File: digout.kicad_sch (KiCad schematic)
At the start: 24 parts, among them J11 EPY.00.250.NTN, J12 EPY.00.250.NTN, J13 EPY.00.250.NTN, J14 EPY.00.250.NTN, U13 SN74LVC8T245PW, U14 SN74LVC8T245PW, U15 SN74LVC8T245PW, U5 SN74LVC8T245PW

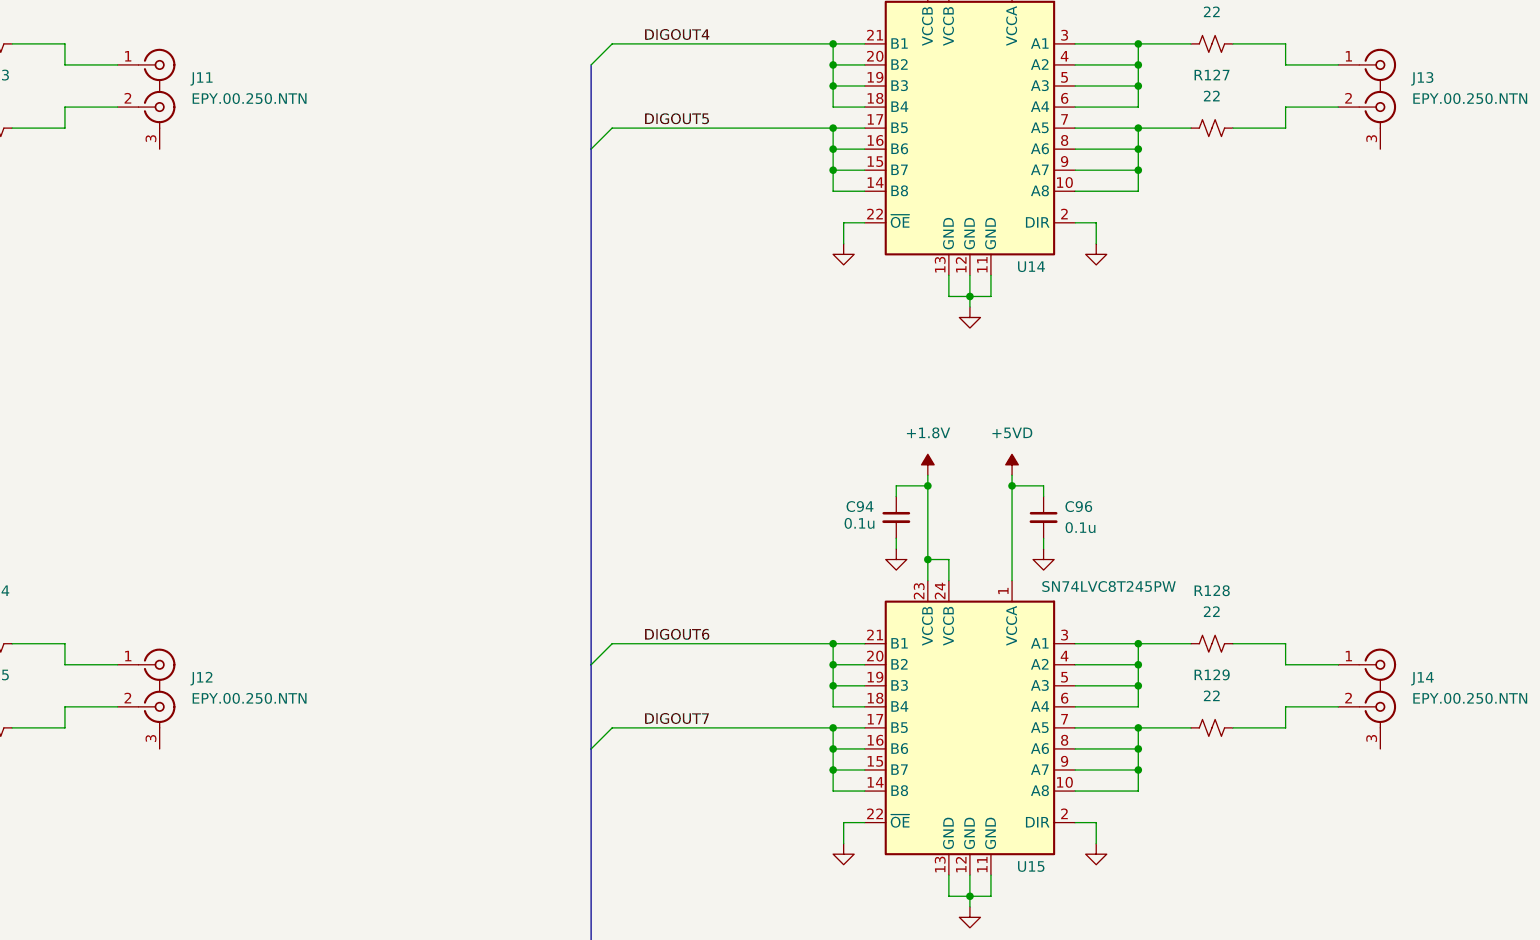
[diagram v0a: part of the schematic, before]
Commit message: Finish board, sent out for quote
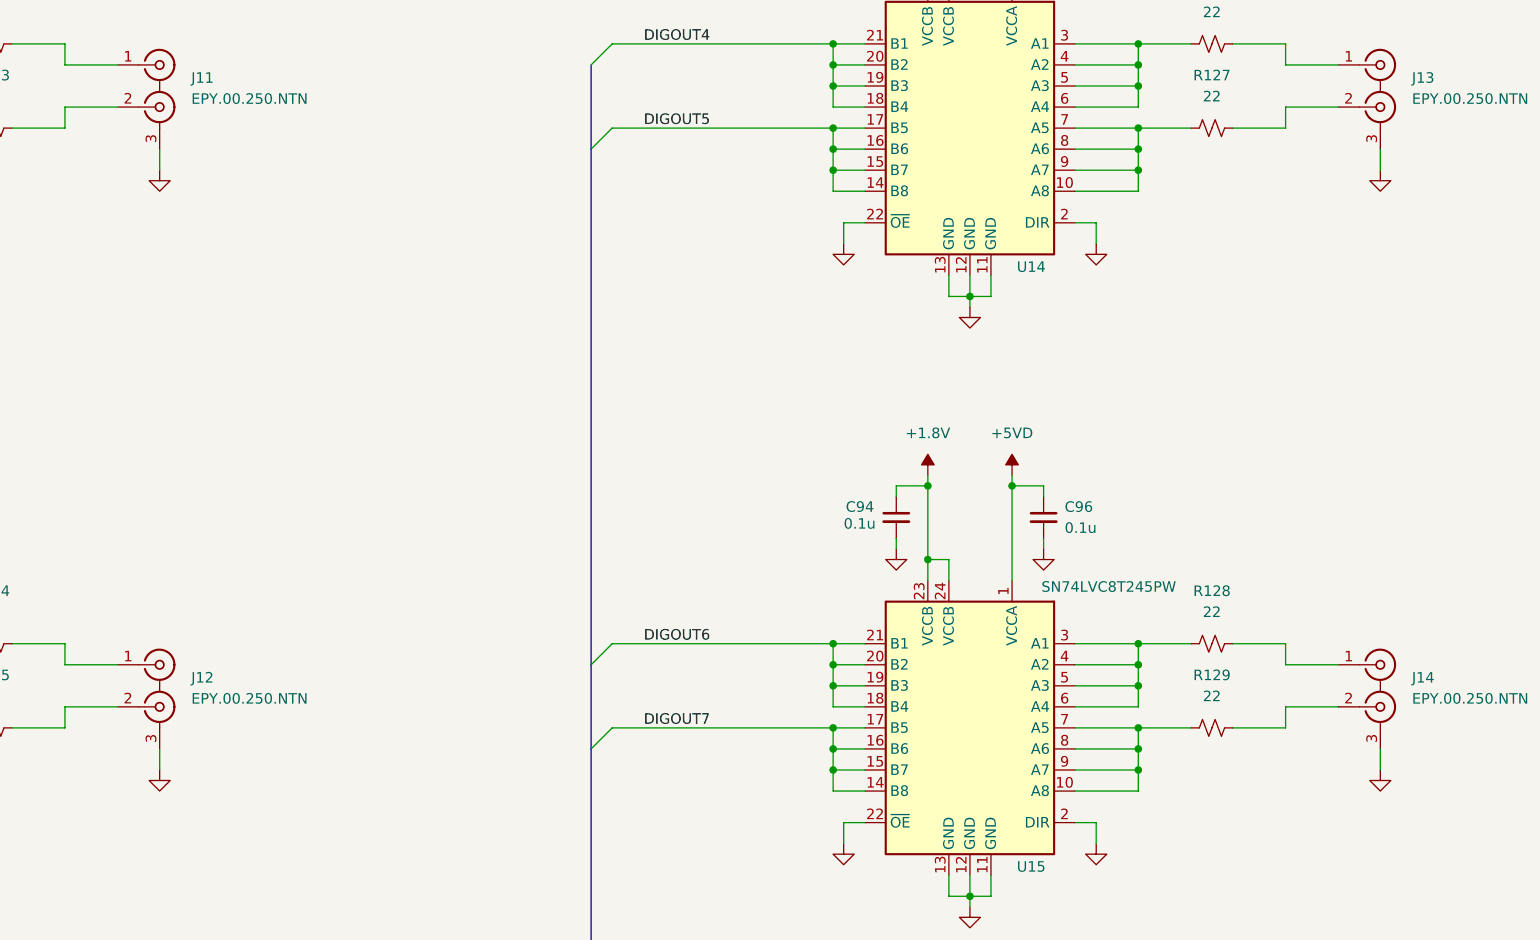
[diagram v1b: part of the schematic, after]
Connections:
- net GND: now also J11.3 (EXT), J12.3 (EXT), J13.3 (EXT), J14.3 (EXT)
